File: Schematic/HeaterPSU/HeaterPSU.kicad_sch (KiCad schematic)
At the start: 62 parts, among them J201 Heater output, J202 To MCU Board, J203 SMPS2_SEC, Q201 SIRA24DP-T1-GE3, Q202 IRF4905, SW201 ALPSALPINE_SRBV_1P5T, U201 XL4005, U202 MCP14A0052T, U203 INA293B, U204 L78L05_SOT89, U205 TS321

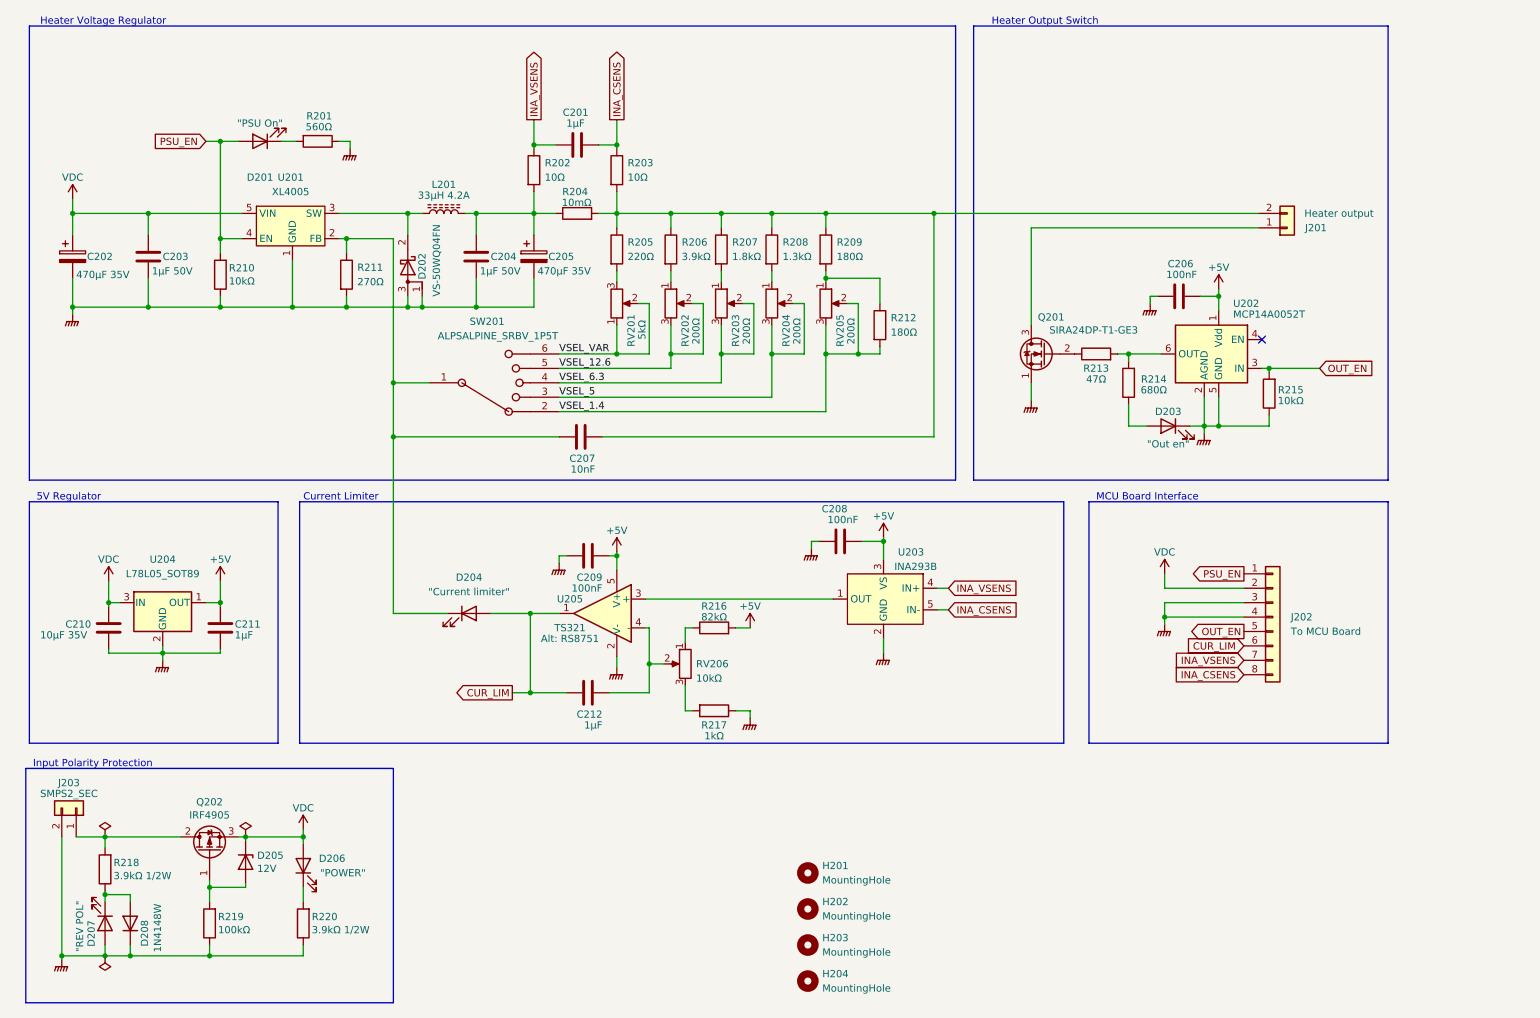
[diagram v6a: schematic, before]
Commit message: Added output filter caps + spacing around mounting holes
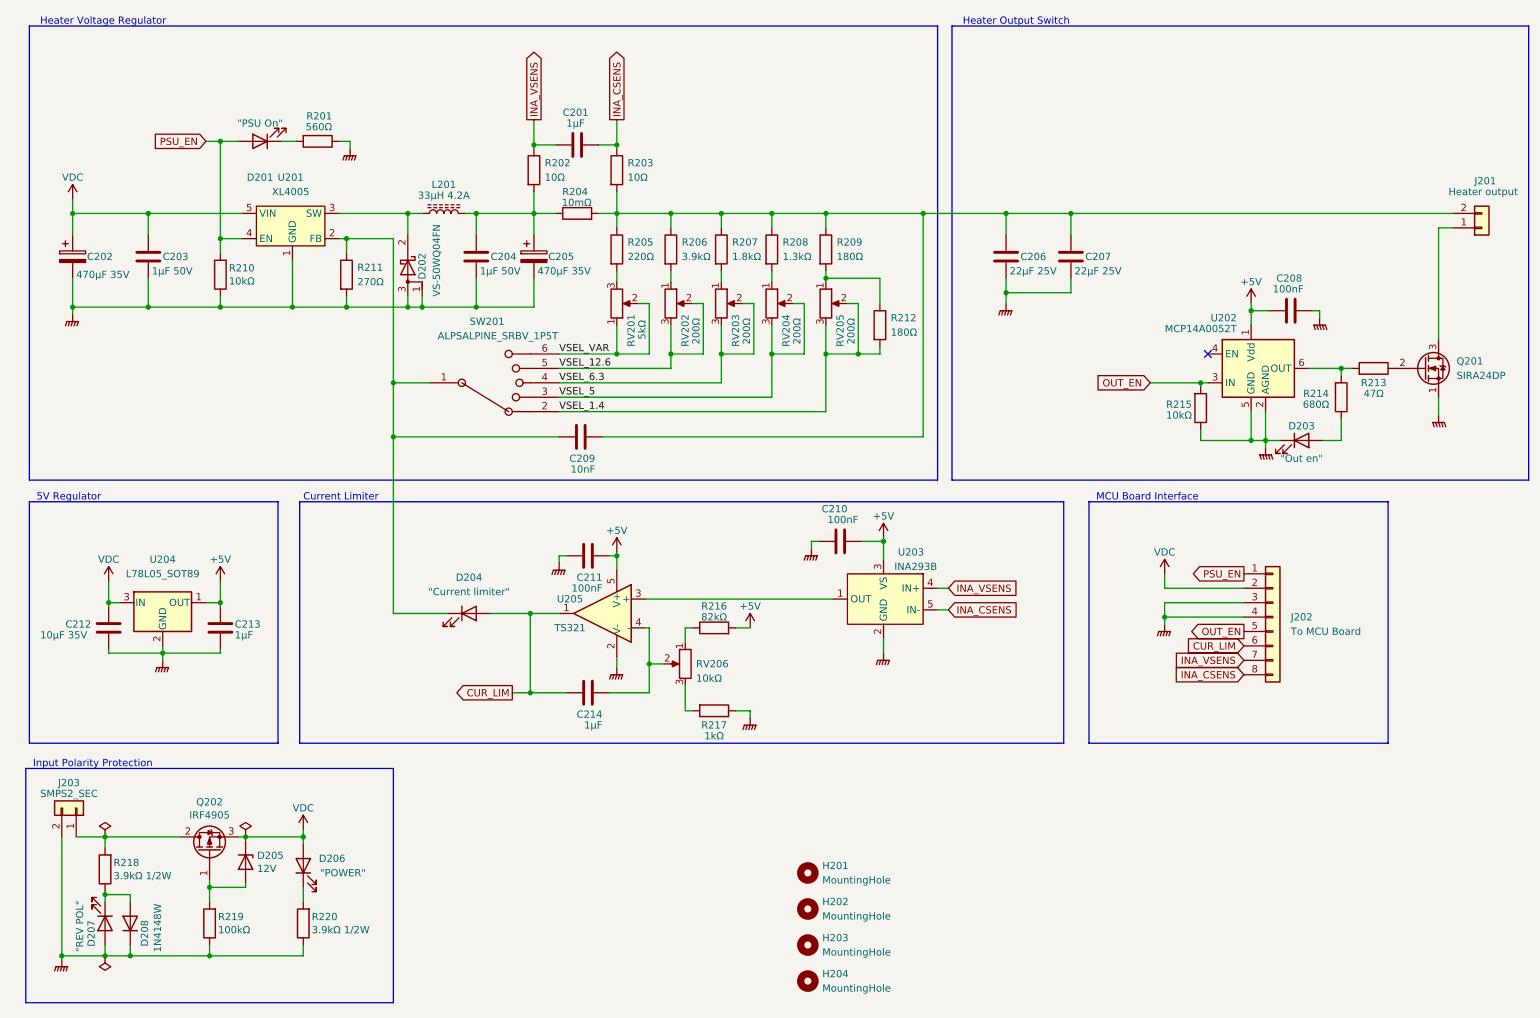
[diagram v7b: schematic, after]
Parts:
- added C206, C207: 22µF 25V, Capacitor_SMD:C_0805_2012Metric_Pad1.18x1.45mm_HandSolder, symbol Device:C
- Q201: value SIRA24DP-T1-GE3 -> SIRA24DP
- U205: Comments Alt: RS8751 -> (none)
- renumbered C206 to C208, C207 to C209, C208 to C210, C209 to C211, C210 to C212, C211 to C213, C212 to C214
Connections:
- net GNDPWR: now also C206.2, C207.2
- net at C209.2, J201.2 (Pin_2), R203.2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: now also C206.1, C207.1
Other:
- moved on the sheet: C208, D203, J201, Q201, R213, R214, R215, U202

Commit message: Changed LED footprints to 0603
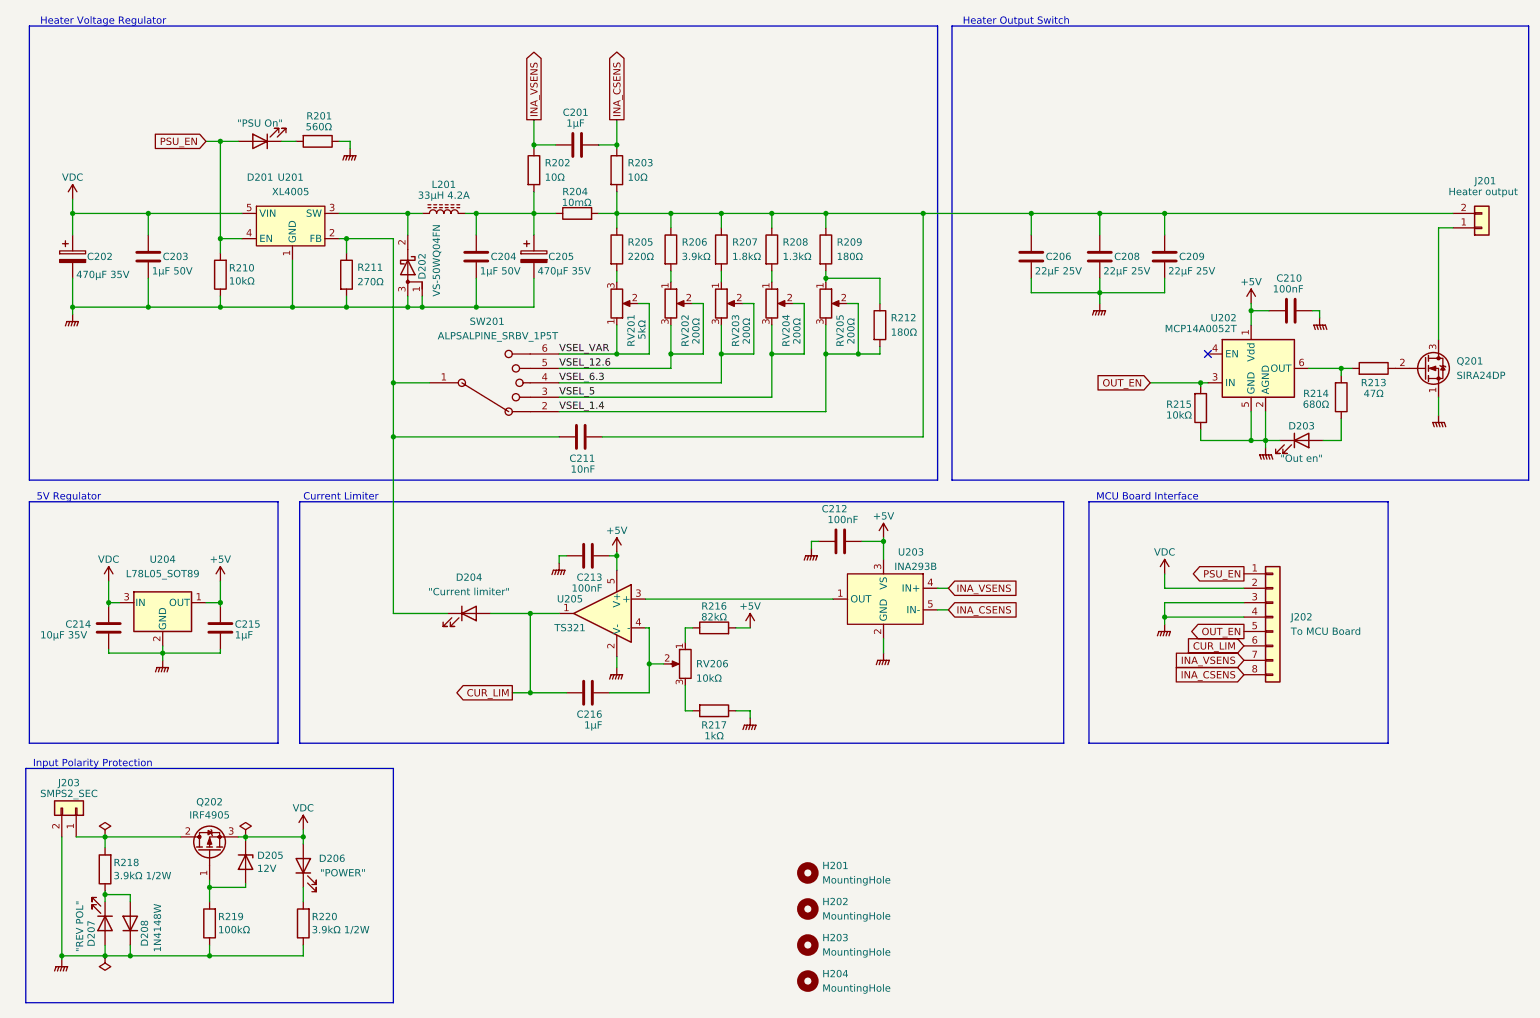
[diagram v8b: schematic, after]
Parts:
- added C206: 22µF 25V, Capacitor_SMD:C_0805_2012Metric_Pad1.18x1.45mm_HandSolder, symbol Device:C
- D201, D203, D204, D206, D207: footprint LED_SMD:LED_0805_2012Metric_Pad1.15x1.40mm_HandSolder -> LED_SMD:LED_0603_1608Metric_Pad1.05x0.95mm_HandSolder
- renumbered C206 to C208, C207 to C209, C208 to C210, C209 to C211, C210 to C212, C211 to C213, C212 to C214, C213 to C215, C214 to C216
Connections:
- net GNDPWR: now also C206.2
- net at C208.1, C209.1, C211.2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: now also C206.1
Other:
- moved on the sheet: C208, C209
